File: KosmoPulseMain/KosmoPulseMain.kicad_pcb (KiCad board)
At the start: 2 copper layers, 170.5 x 44 mm, 47 parts, among them J1 OUT6, J10 OUT12, J11 OUT24, J2 OUT4, J3 OUT2, J4 OUT1, J5 OUT3, J6 OUT7, J7 OUT5, J8 1247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

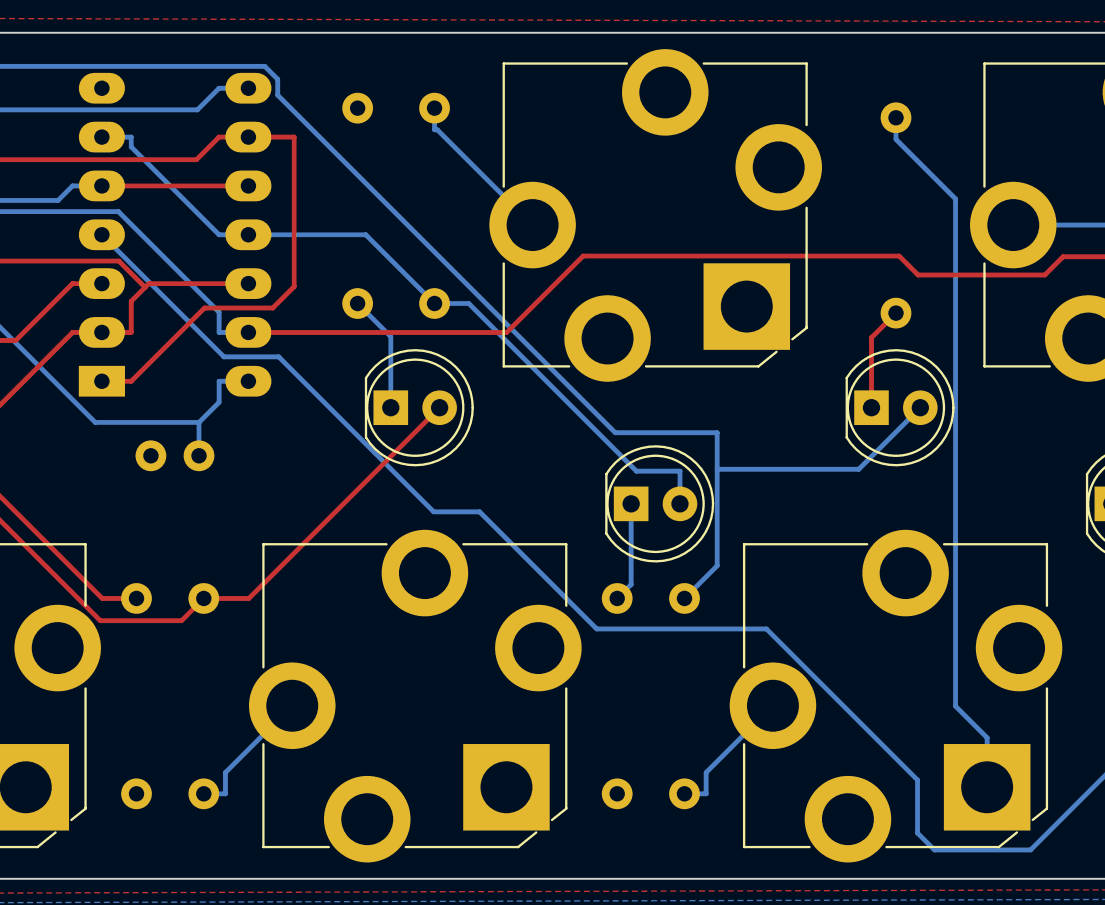
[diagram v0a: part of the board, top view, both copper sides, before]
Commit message: Added GND to BIT 6
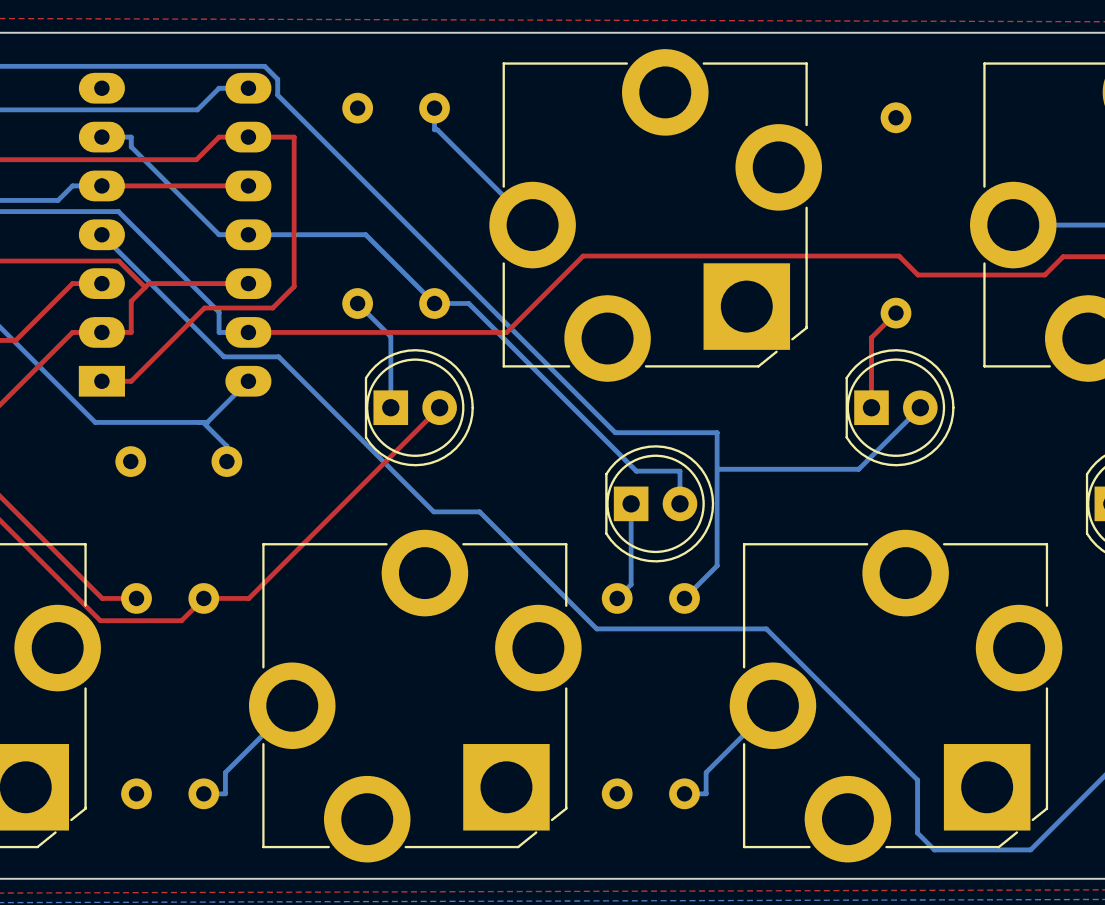
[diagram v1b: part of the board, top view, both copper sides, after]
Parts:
- C1: footprint ao_tht:C_Disc_D3.0mm_W1.6mm_P2.50mm -> ao_tht:C_Rect_L7.2mm_W2.5mm_P5.00mm_FKS2_FKP2_MKS2_MKP2
- moved C1 1.48 mm to (165.2, 125.3)
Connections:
- J1 pad S: Net-(J1-PadS) -> GND
- R12 pad 2: Net-(J1-PadS) -> GND
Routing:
- net Net-(J1-PadS): track 36.8 -> 0.00 mm
